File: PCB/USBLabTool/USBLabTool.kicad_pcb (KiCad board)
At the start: 4 copper layers, 79.4 x 56.2 mm, 228 parts, among them J1 Conn_01x06_Pin, J10 T_pwm, J11 T_buf, J12 T_buf, J13 ADC2, J14 ADC1, J15 +3.3VA, J16 +3.3VA, J17 2x01, J19 T_N5V, J2 Conn_02x12_Odd_Even, J20 USB_C_Receptacle, J3 T_att, J4 T_att, J5 T_acdc, J6 T_acdc, J7 T_amp, J8 T_amp, J9 T_pwm, K1 G5V-2, K2 G5V-2, Q1 STL11N3LLH6, SW1 SW_Push, U1 AQY284SX, U10 Opamp_Quad, U11 DG403, U12 STM32H562VGTx, U13 r1283, U14 ST1L05APU33R, U15 ST1L05APU33R, U16 LTC1983ES6-5#TRPBF, U17 TCPP01-M12, U18 74HC245, U2 AQY284SX, U20 74HC245, U3 CD74HC4316PWR, U4 LMP7718, U5 CD74HC4316PWR, U6 LMP7718, U7 OPA863, U8 OPA863, U9 Opamp_Quad, Y1 32.768kHz

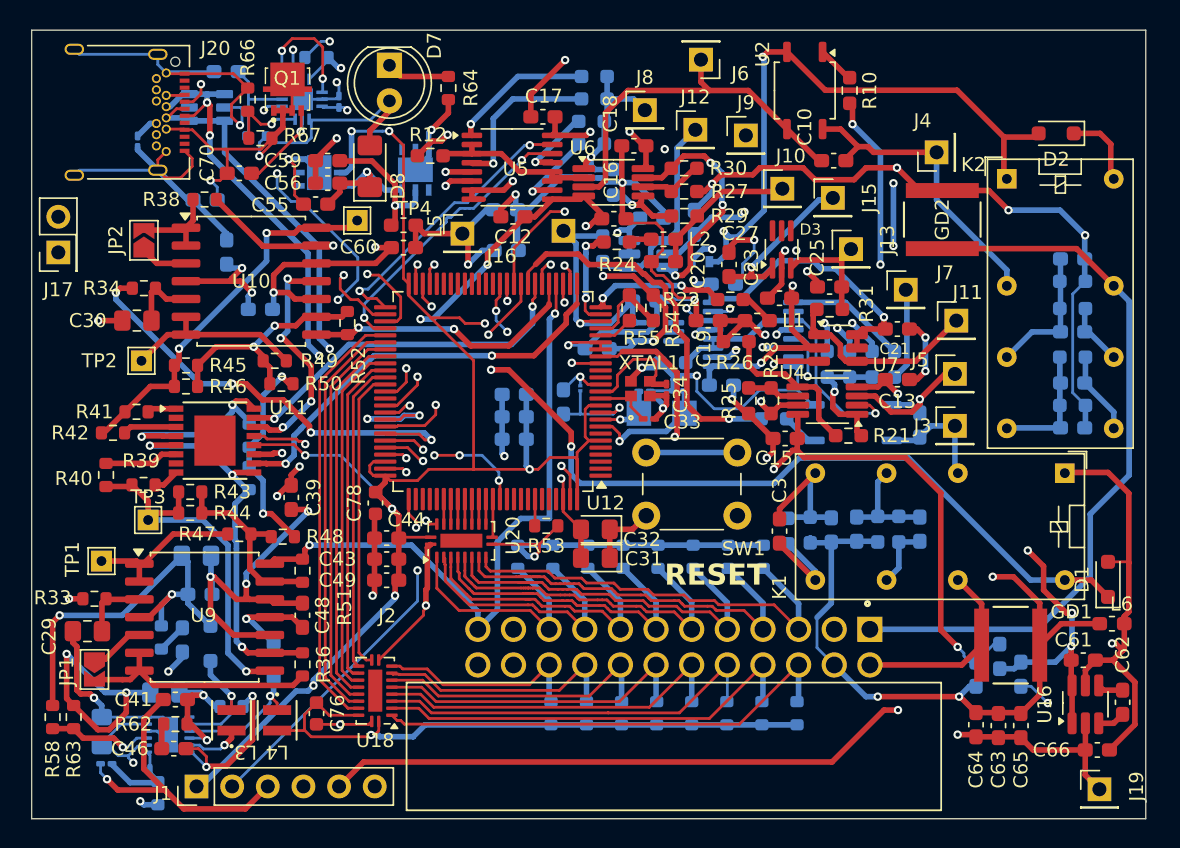
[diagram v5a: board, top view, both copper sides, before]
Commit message: Added holes to PCB schematic, fixed DRC
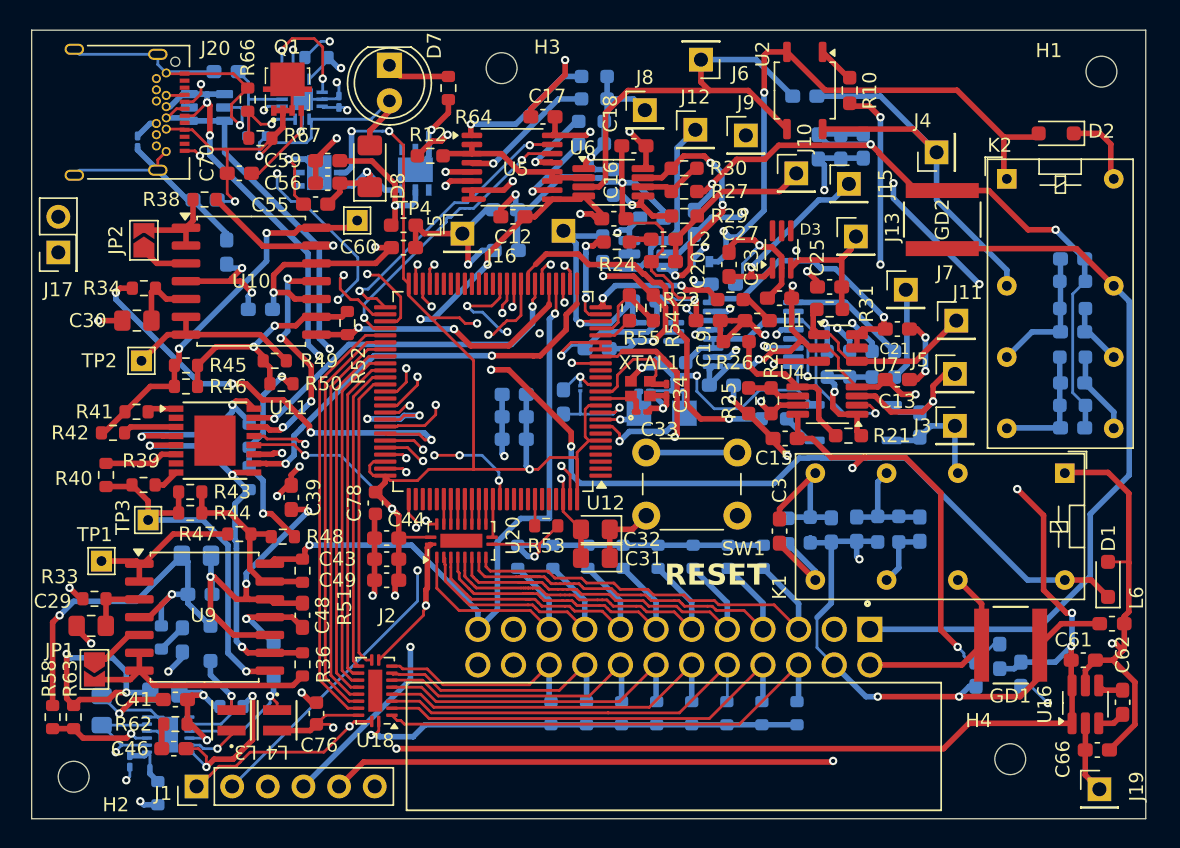
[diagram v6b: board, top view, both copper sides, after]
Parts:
- added H1: MountingHole, MountingHole:MountingHole_2.2mm_M2, F.Cu at (186.2, 68.5)
- added H2: MountingHole, MountingHole:MountingHole_2.2mm_M2, F.Cu at (113.0, 118.8)
- added H3: MountingHole, MountingHole:MountingHole_2.2mm_M2, F.Cu at (143.5, 68.2)
- added H4: MountingHole, MountingHole:MountingHole_2.2mm_M2, F.Cu at (179.8, 117.5)
- C10, C63, C64, C65: moved to B.Cu
- moved C65 43.7 mm to (166.1, 73.9)
- moved C63 42.7 mm to (167.7, 73.9)
- moved C64 42.0 mm to (169.3, 73.8)
- moved C10 5.04 mm to (165.1, 70.2)
- moved C42 1.68 mm to (117.0, 117.7), turned to -90 degrees
- moved J15 1.52 mm to (168.2, 76.5)
- moved C37 1.50 mm to (115.0, 114.0)
- moved J10 1.48 mm to (164.5, 75.8)
- moved J13 0.97 mm to (168.8, 80.2)
- moved C33 0.71 mm to (153.5, 92.8)
- moved C29 0.46 mm to (114.2, 108.0)
- turned C76 to -90 degrees
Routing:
- net GND: track 353.2 -> 323.5 mm, vias 28 -> 31
- net +5V: track 265.4 -> 238.8 mm
- net Net-(J4-Pin_1): track 21.8 -> 30.6 mm
- net +5VCLEAN: track 97.8 -> 92.9 mm
- net CH1_amp_1: track 24.2 -> 19.8 mm
- net Net-(J6-Pin_1): track 27.1 -> 31.3 mm
- net CH1_amp_2.5: track 31.4 -> 35.3 mm
- net -5V: track 143.0 -> 146.0 mm
- net Net-(U13-Vref): track 6.31 -> 3.72 mm
- net Net-(U5-2Z): track 11.6 -> 9.74 mm
- net Net-(J10-Pin_1): track 10.5 -> 12.3 mm
- net +3.3V: track 139.3 -> 141.0 mm
- net +3.3VA: track 55.4 -> 57.0 mm
- net GNDA: track 334.5 -> 335.8 mm, vias 27 -> 25
- net Net-(U13-Vfb1): track 16.1 -> 14.9 mm
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
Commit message: some more minor PCB changes
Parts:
- moved C17 1.82 mm to (148.2, 71.5), turned to 0 degrees
- moved C11 0.47 mm to (159.6, 90.8)
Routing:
- net GNDA: track 335.8 -> 307.4 mm, vias 25 -> 27
- net GND: track 323.5 -> 307.7 mm, vias 31 -> 30
- net UCPD_CC1: track 36.3 -> 37.9 mm
- net +5V: track 238.8 -> 240.2 mm
- net CH0_attenuate: track 51.9 -> 50.8 mm
- net Net-(U6-OUT_B): track 16.6 -> 17.6 mm
- net Net-(U5-1Z): track 10.1 -> 9.55 mm
